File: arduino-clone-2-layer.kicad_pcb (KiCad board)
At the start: 4 copper layers, 42.2 x 27.7 mm, 17 parts, among them J1 Serial, J2 Digital Pins, J3 ICSP, J4 I2C, U1 24LC1025, U2 24LC1025, U3 DS13375+, U4 ATMEGA328P-AU, Y1 Crystal 32MHz, Y2 Crystal 16MHz

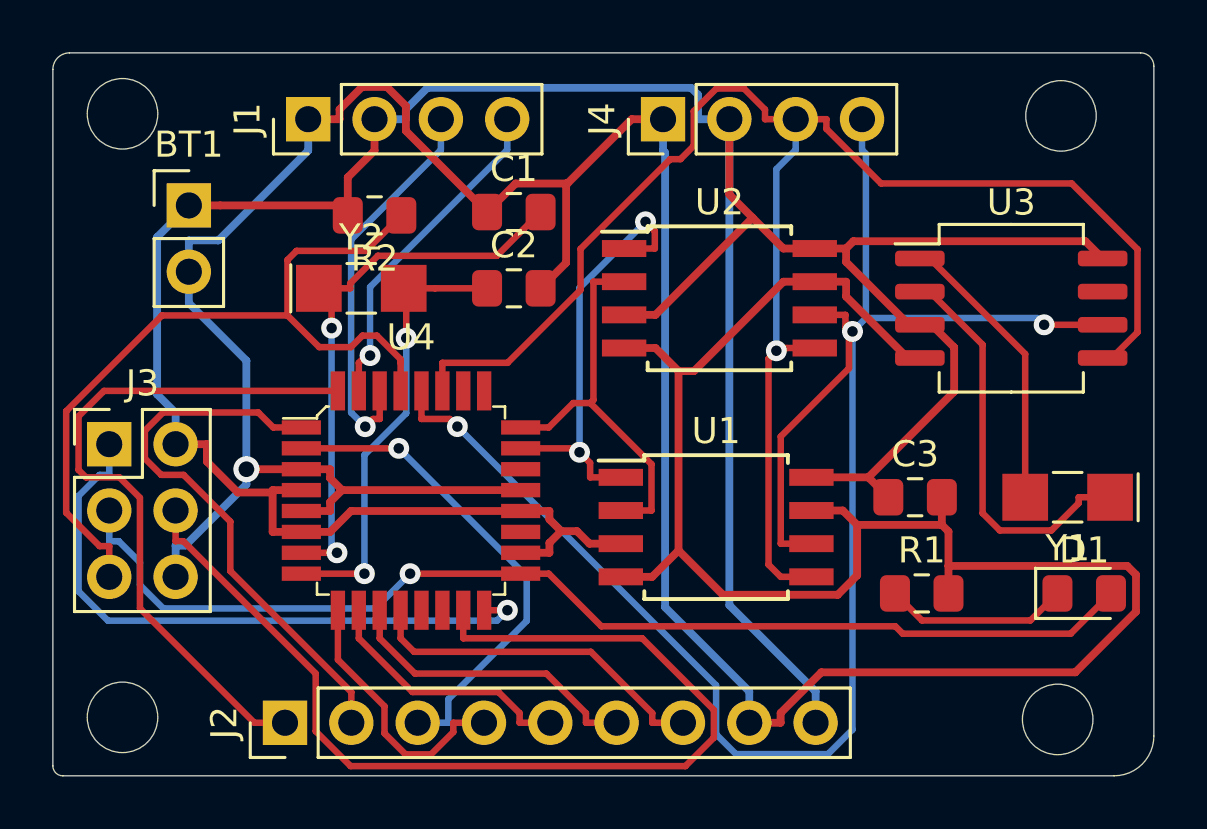
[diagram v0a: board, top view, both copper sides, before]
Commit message: [pcbnew] add 2 and 4 layer autorouted pcbs
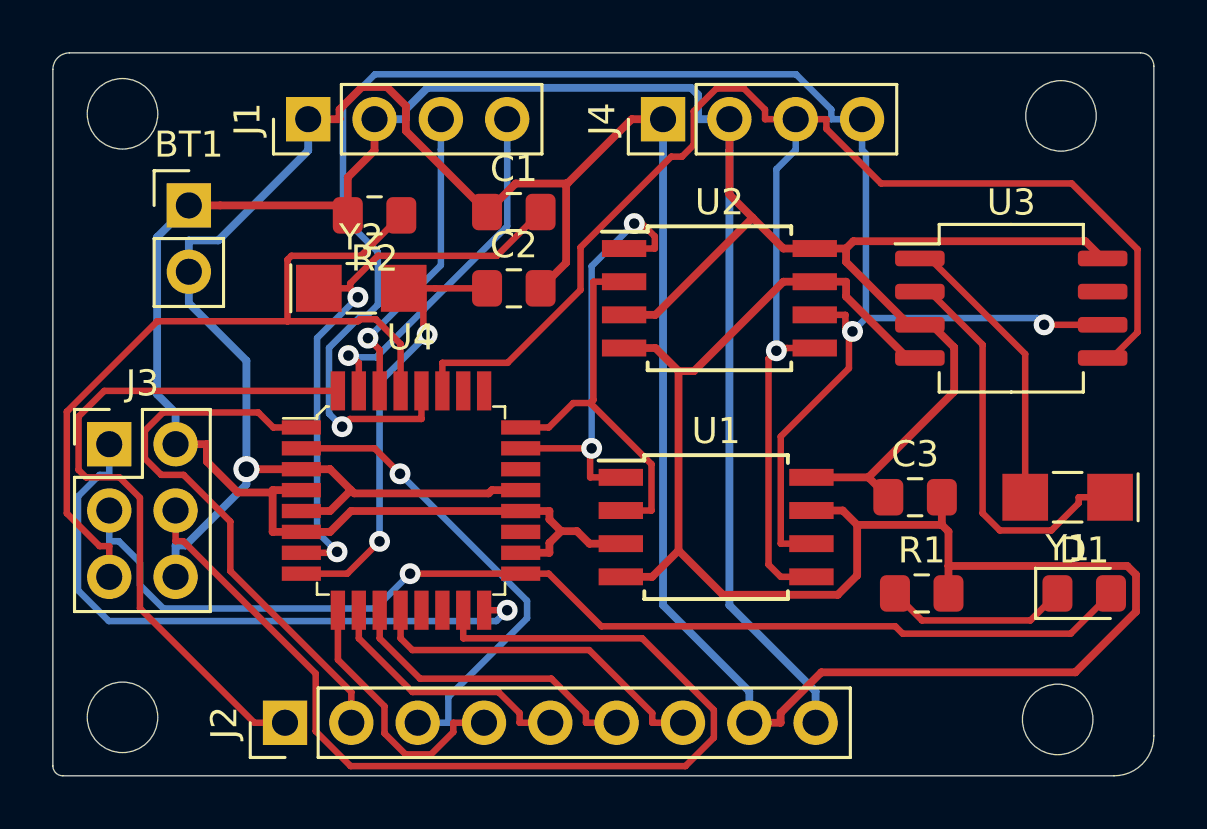
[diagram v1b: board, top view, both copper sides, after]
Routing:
- net /RX: track 15.2 -> 11.7 mm
- net /TX: track 12.8 -> 13.9 mm
- net Net-(C1-Pad2): track 21.4 -> 22.4 mm
- net /D4: track 18.7 -> 18.2 mm
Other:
- copper layers 4 -> 2
